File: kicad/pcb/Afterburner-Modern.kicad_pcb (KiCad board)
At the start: 2 copper layers, 100 x 100 mm, 44 parts, among them J1 USB_C_Receptacle_HRO_TYPE-C-3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, J2 TerminalBlock_MaiXu_MX126-5.0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, J3 JST_XH_B3B-XH-A_1x03_P2.50mm_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, J4 JST_XH_B3B-XH-A_1x03_P2.50mm_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, J5 JST_XH_B4B-XH-A_1x04_P2.50mm_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, SW1 SW_Push_1TS009xxxx-xxxx-xxxx_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, SW2 SW_Push_1TS009xxxx-xxxx-xxxx_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, U1 QFN-44-1EP_7x7mm_P0.5mm_EP5.2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, U10 QFN-24-1EP_4x4mm_P0.5mm_EP2.5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, U11 Hirose_FH12-18S-0.5SH_1x18-1M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, U2 SOT-23-6, U3 SOT-89-3, U4 DFN-8-1EP_2x2mm_P0.5mm_EP0.9x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, U7 SOIC-16_3.9x9.9mm_P1.27mm, U8_1 SOT-23, U8_2 SOT-23, U9 SOIC-14_3.9x8.7mm_P1.27mm

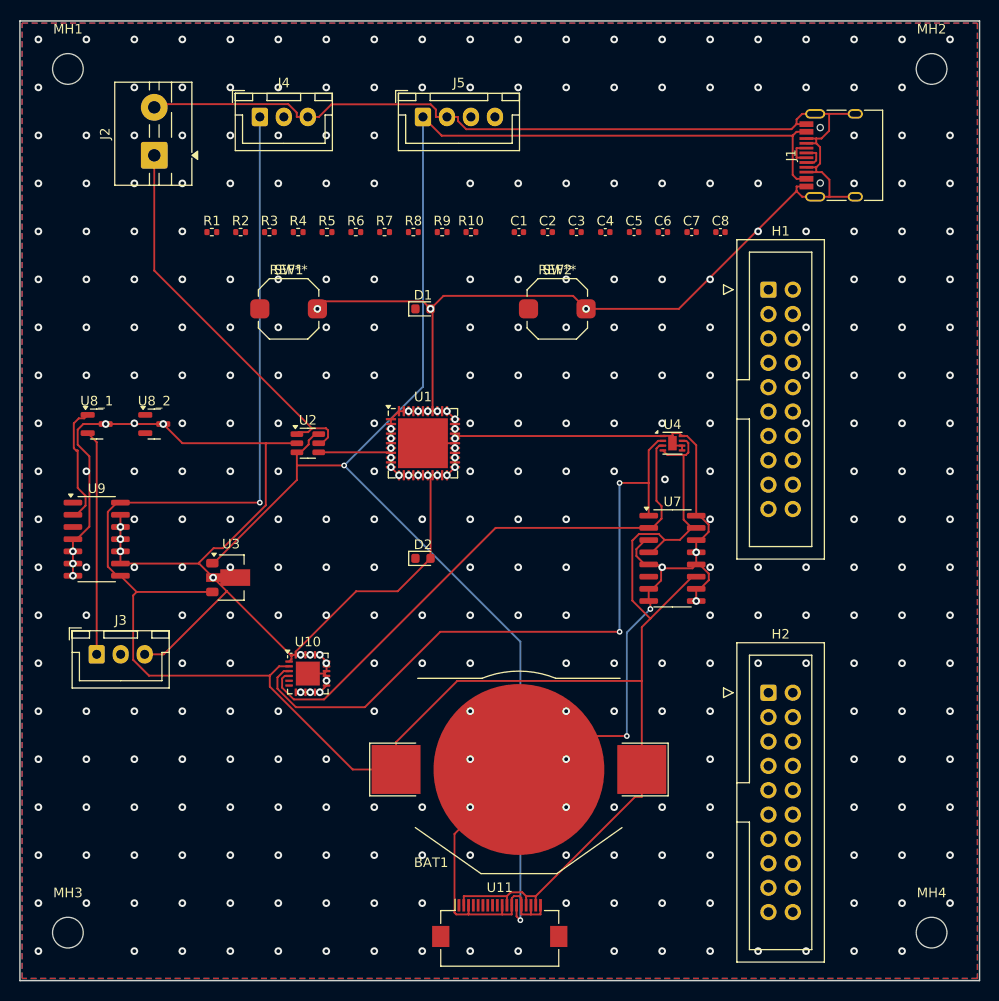
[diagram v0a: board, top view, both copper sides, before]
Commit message: feat(kicad): account for ILI9341 display and side buttons across board, case, docs
Board (pipeline.py):
- Relocate SW1/SW2 to right-angle (side-actuated) PTS645 tactiles on the front
  edge so they're pressed from the case side, off the display footprint.
- Add a lid-mounted ILI9341 keepout (module + active area + label) on Dwgs.User.
- Fixes: fall back to in-memory board when headless LoadBoard returns None;
  set PCB_SHAPE/PCB_TEXT layers after Add (were serialized as UNDEFINED, which
  made boards unloadable); honest run_drc on load failure; runtime probe for
  ZONE_FILLER so GND zones fill where supported and are left defined-unfilled
  (fill in KiCad) where the headless filler would crash.

Case (case/generate_case.py): lid display window + recessed glass pocket with
bezel ledge, retaining rib and FPC notch; side-button plunger holes; standoffs
raised to 10mm for B.Cu connector clearance.

Renders: board top/iso/bottom + case base/lid views. Docs updated for the
100x100 board, lid-mounted display, and side buttons.

Co-Authored-By: Claude Opus 4.8 <noreply@anthropic.com>
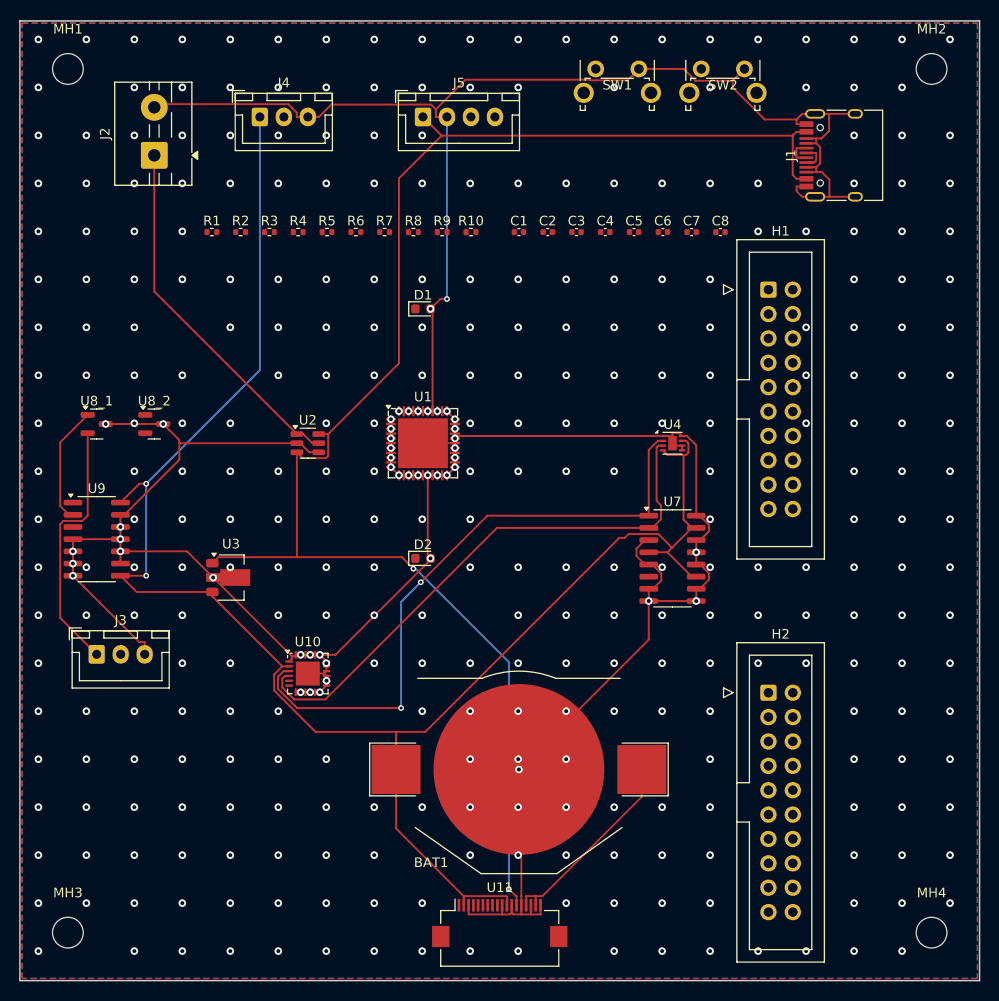
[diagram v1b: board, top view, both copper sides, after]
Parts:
- SW1, SW2: value SW_Push_1TS009xxxx-xxxx-xxxx_6x6x5mm -> SW_Tactile_SPST_Angled_PTS645Vx39-2LFS; footprint SW_Push_1TS009xxxx-xxxx-xxxx_6x6x5mm -> SW_Tactile_SPST_Angled_PTS645Vx39-2LFS
- moved SW1 40.6 mm to (60.0, 5.00)
- moved SW2 29.2 mm to (71.0, 5.00)
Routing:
- net GND: track 461.3 -> 397.4 mm, vias 367 -> 372
- net 3V3: track 231.7 -> 206.2 mm, vias 1 -> 2
- net 5V: track 166.6 -> 161.8 mm
- net I2C_SDA: track 69.6 -> 65.6 mm
- net BLUE_TX_H: track 23.4 -> 27.0 mm
- net 12V: track 40.8 -> 37.9 mm
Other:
- board text added: "ILI9341 2.8" (lid-mounted)"
